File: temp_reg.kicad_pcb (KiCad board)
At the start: 2 copper layers, 72.4 x 57.1 mm, 43 parts, among them P1 CONN_01X02, P11 CONN_2, P13 CONN_2, P2 CONN_01X04, P3 CONN_2, P6 CONN_01X01, P7 CONN_01X01, P8 CONN_01X01, P9 CONN_01X01, U1 OPA547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

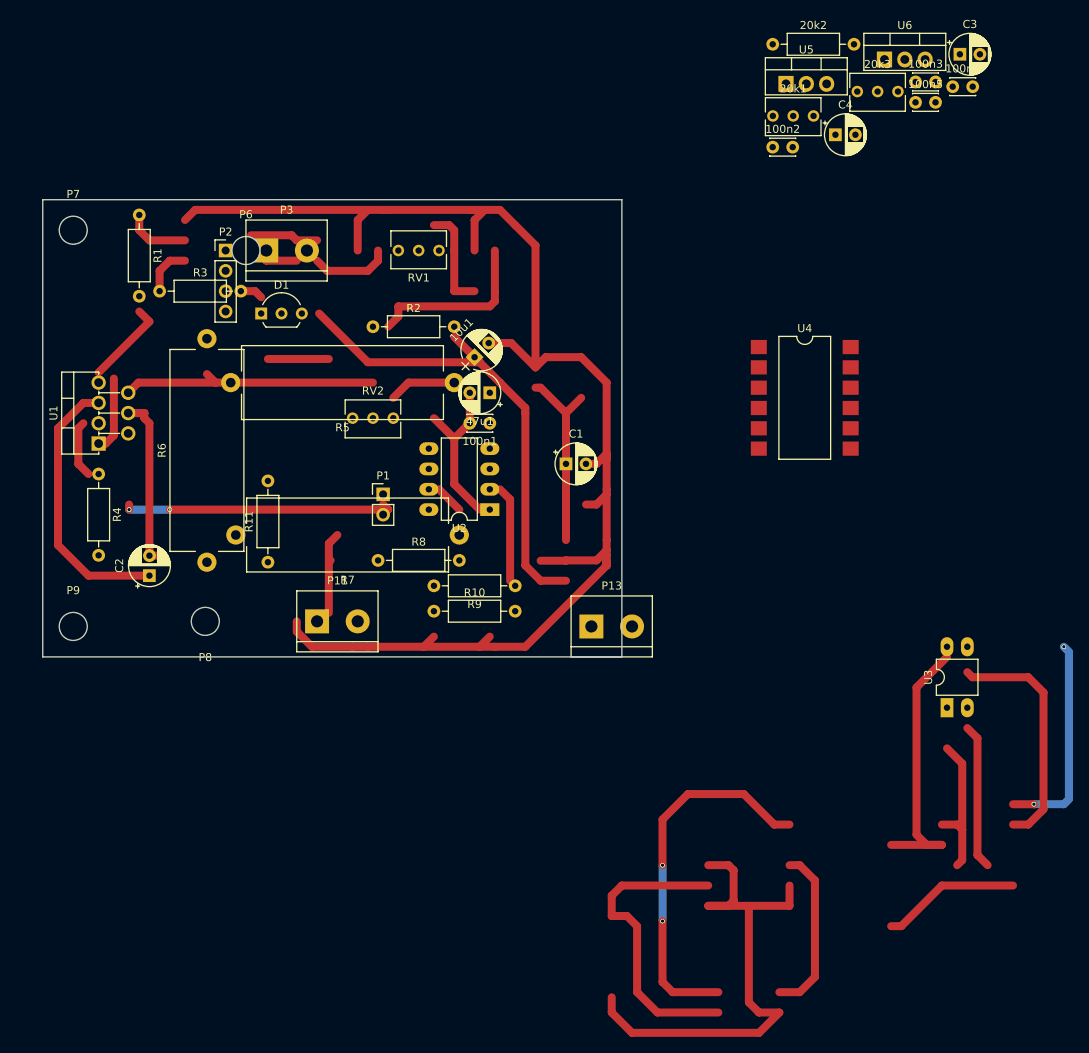
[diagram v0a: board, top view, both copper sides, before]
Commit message: finished pcbart
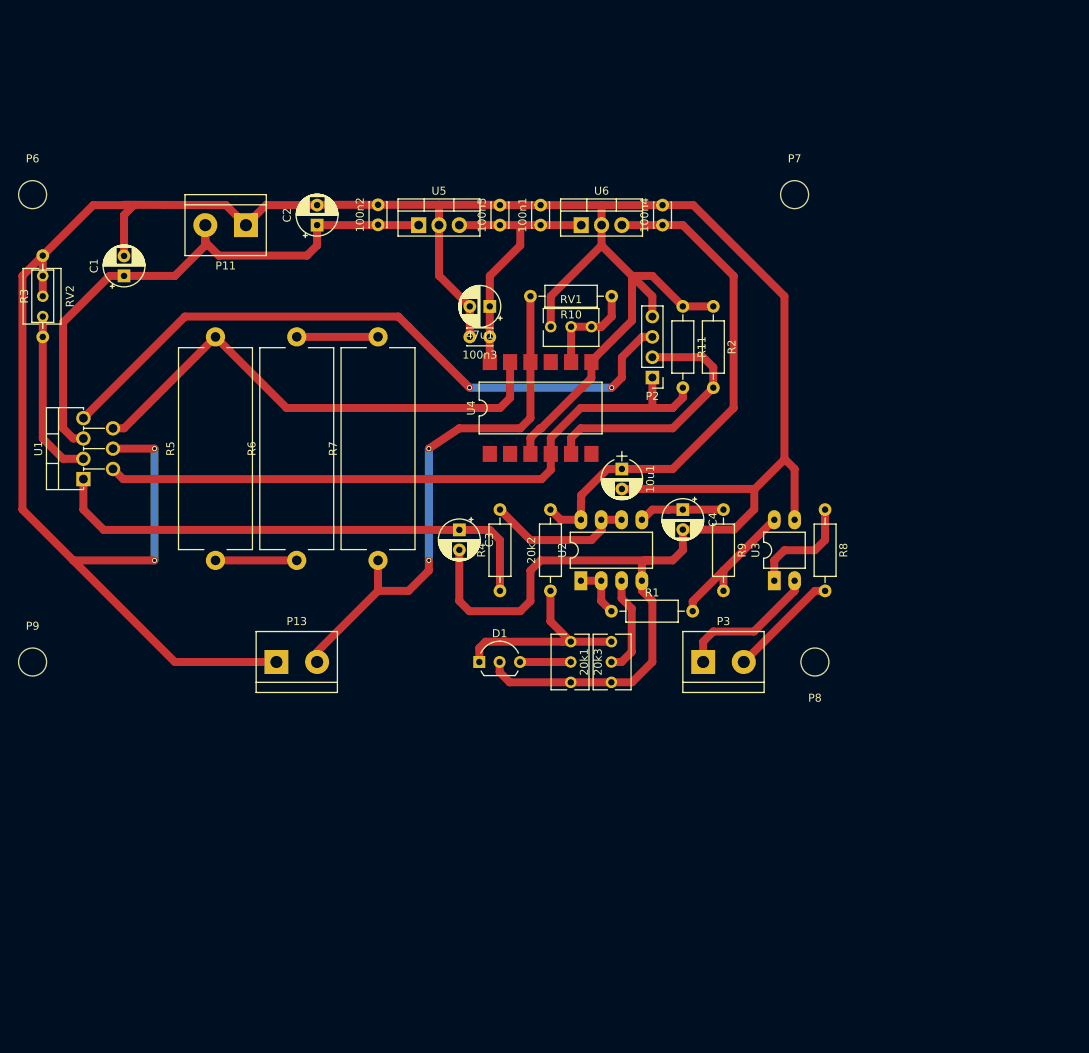
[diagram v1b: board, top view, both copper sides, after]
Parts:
- removed P1: CONN_01X02, Connector_PinHeader_2.54mm:PinHeader_1x02_P2.54mm_Vertical
- moved P7 90.3 mm to (109.2, 14.0)
- moved C3 86.3 mm to (67.3, 55.9), turned to 270 degrees
- moved 20k3 84.4 mm to (81.2, 74.9), turned to 270 degrees
- moved R1 77.0 mm to (86.3, 66.0), turned to 0 degrees
- moved P8 76.4 mm to (111.8, 72.4)
- moved P3 75.0 mm to (97.8, 72.4)
- moved 20k2 73.8 mm to (78.7, 63.5), turned to 90 degrees
- moved 20k1 70.4 mm to (86.3, 69.8), turned to 90 degrees
- moved 100n3 62.0 mm to (71.1, 31.8), turned to 180 degrees
- moved R11 60.9 mm to (95.2, 27.9), turned to 270 degrees
- moved C1 60.0 mm to (25.4, 24.1), turned to 90 degrees
- moved R8 56.2 mm to (113.0, 53.3), turned to 270 degrees
- moved P2 55.7 mm to (91.4, 36.8), turned to 180 degrees
- moved 100n5 54.2 mm to (72.4, 17.8), turned to 90 degrees
- moved R4 52.2 mm to (72.4, 63.5), turned to 90 degrees
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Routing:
- net (no net): track 189.1 -> 0.00 mm, vias 2 -> 0
- net GNDPWR: track 306.5 -> 444.7 mm
- net /tmon: track 0.00 -> 84.2 mm, vias 0 -> 2
- net Net-(C3-Pad1): track 18.0 -> 63.8 mm
- net /pmon: track 41.5 -> 83.4 mm
- net Net-(P13-Pad2): track 29.8 -> 66.5 mm, vias 0 -> 2
- net +12V: track 0.00 -> 33.9 mm
- net /imon: track 0.00 -> 33.1 mm
- net Vref: track 0.00 -> 26.0 mm
- net Net-(D2-Pad1): track 21.7 -> 0.00 mm
- net Net-(R4-Pad2): track 0.00 -> 18.6 mm
- net Net-(R1-Pad2): track 0.00 -> 18.2 mm
- net +48V: track 57.7 -> 73.2 mm
- net Net-(R3-Pad1): track 6.24 -> 21.4 mm
- net Net-(P3-Pad2): track 0.00 -> 13.8 mm
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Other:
- board outline removed
